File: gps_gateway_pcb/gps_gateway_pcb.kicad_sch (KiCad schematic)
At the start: 76 parts, among them J1 USB_OTG, J2 4G, J3 EG800, J4 Conn_01x03_Pin, J5 Conn_01x06_Pin, J7 SIM_Card, Q1 DTC143Z, Q2 DTC143Z, Q3 DTC143Z, Q6 2SC4617TLQ, Q7 2SC4617TLQ, SW1 RST, SW2 Boot, U1 GNSS, U2 TPS54202DDC, U3 RT9013-33GB, U4 Main, U5 ESP32-C3FH4, Y1 40MHz

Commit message: layout done go to prototype
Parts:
- removed C1, C3: 100nF, Capacitor_SMD:C_0603_1608Metric, symbol Device:C_Small
- removed C11: 10nF, Capacitor_SMD:C_0603_1608Metric, symbol Device:C
- removed C16: 10nF, Capacitor_SMD:C_0603_1608Metric, symbol Device:C_Small
- removed C17, C25: 0.1uF, Capacitor_SMD:C_0603_1608Metric, symbol Device:C_Small
- removed C23, C24: 1nF, Capacitor_SMD:C_0603_1608Metric, symbol Device:C_Small
- removed C5: 470uF, Capacitor_Tantalum_SMD:CP_EIA-7343-20_Kemet-V, symbol Device:C_Polarized_Small
- removed D4: SS34, Diode_SMD:D_SMA, symbol Diode:SS34
- removed F1: 0.35A, Fuse:Fuse_1206_3216Metric, symbol Device:Fuse_Small
- removed J4: Conn_01x03_Pin, Connector_PinHeader_1.27mm:PinHeader_1x03_P1.27mm_Vertical, symbol Connector:Conn_01x03_Pin
- removed J7: SIM_Card, UserLibrary:SIM-SMD_WL-SIM150-085, symbol UserLibrary:SIM_Card_WL-SIM150-085
- removed Q1, Q2, Q3: DTC143Z, Package_TO_SOT_SMD:SOT-416, symbol Transistor_BJT:DTC143Z
- removed Q7: 2SC4617TLQ, Package_TO_SOT_SMD:SOT-416, symbol Device:Q_NPN_BEC
- removed R1, R2: 10K, Resistor_SMD:R_0603_1608Metric, symbol Device:R
- removed R17, R20, R76: 0, Resistor_SMD:R_0603_1608Metric, symbol Device:R_Small_US
- removed R6: 100K, Resistor_SMD:R_0603_1608Metric, symbol Device:R_Small
- removed R7: 4K7, Resistor_SMD:R_0603_1608Metric, symbol Device:R
- removed R74: 10K, Resistor_SMD:R_0603_1608Metric, symbol Device:R_Small_US
- removed R8: 3K3, Resistor_SMD:R_0603_1608Metric, symbol Device:R_Small
- removed R9: 22.1K, Resistor_SMD:R_0603_1608Metric, symbol Device:R_Small
- removed SW1: RST, Button_Switch_SMD:SW_Push_SPST_NO_Alps_SKRK, symbol User Library:SW_Push
- removed SW2: Boot, Button_Switch_SMD:SW_Push_SPST_NO_Alps_SKRK, symbol User Library:SW_Push
- removed U1: GNSS, Connector_Coaxial:U.FL_Hirose_U.FL-R-SMT-1_Vertical, symbol UserLibrary:Antenna_IPEX
- removed U3: RT9013-33GB, Package_TO_SOT_SMD:TSOT-23-5, symbol UserLibrary:RT9013-33GB
- added C19: 10uF, Capacitor_SMD:C_0603_1608Metric, symbol Device:C_Small
- added D2, D3: 1N5819W, Diode_SMD:D_SOD-123, symbol Diode:SS34
- added D6: LED, LED_THT:LED_D3.0mm, symbol Device:LED
- added H1, H2: MountingHole_Pad, MountingHole:MountingHole_2.7mm_M2.5_DIN965_Pad, symbol Mechanical:MountingHole_Pad
- added J3: GNSS, Connector_Coaxial:U.FL_Hirose_U.FL-R-SMT-1_Vertical, symbol Connector:Conn_Coaxial_Small
- added J7: SIM_Card, UserLibrary:nanoSIM_ConnMold_CMNSM661004, symbol UserLibrary:SIM_Card_CD
- added JP1: SolderJumper_3_Open, Jumper:SolderJumper-3_P1.3mm_Open_Pad1.0x1.5mm, symbol Jumper:SolderJumper_3_Open
- added Q3: SS8050, Package_TO_SOT_SMD:SOT-23, symbol Device:Q_NPN_BEC
- added R1: 0R, Resistor_SMD:R_0603_1608Metric, symbol Device:R_Small_US
- added R10, R24, R25, R26, R6, R7, R8: 10K, Resistor_SMD:R_0603_1608Metric, symbol Device:R_Small_US
- added R2: 100K, Resistor_SMD:R_0603_1608Metric, symbol Device:R_Small_US
- added R3, R9: 4K7, Resistor_SMD:R_0603_1608Metric, symbol Device:R_Small_US
- added R5: 16K9, Resistor_SMD:R_0603_1608Metric, symbol Device:R_Small_US
- added TP1, TP2, TP3, TP4: TestPoint, TestPoint:TestPoint_Pad_D1.0mm, symbol Connector:TestPoint
- added U4: RT9013-33GB, Package_TO_SOT_SMD:TSOT-23-5, symbol UserLibrary:RT9013-33GB
- C1: renamed from C10; value 1uF -> 10uF
- C14: value 47uF -> 0.1uF; footprint Capacitor_SMD:C_1206_3216Metric -> Capacitor_SMD:C_0603_1608Metric; LCSC C403725 -> C1591
- C4: renamed from C2; value 0.1uF -> 10nF
- D1: value SS34 -> 1N5819W; footprint Diode_SMD:D_SMA -> Diode_SMD:D_SOD-123
- J1: renamed from J5; footprint (none) -> TerminalBlock_Phoenix:TerminalBlock_Phoenix_MPT-0,5-6-2.54_1x06_P2.54mm_Horizontal
- L2: renamed from L4; footprint Inductor_SMD:L_APV_ANR3015 -> Inductor_SMD:L_APV_ANR5040
- L3: footprint Inductor_SMD:L_0603_1608Metric -> Inductor_SMD:L_0402_1005Metric
- Q2: renamed from Q6; value 2SC4617TLQ -> SS8050; footprint Package_TO_SOT_SMD:SOT-416 -> Package_TO_SOT_SMD:SOT-23; LCSC Part #  C308648 -> (none); Mfr. Part #  2SC4617TLQ -> SS8050
- R12: renamed from R4; value 2.2K -> 4K7
- R13: renamed from R5; value 2.2K -> 4K7
- R17: renamed from R13; value 4.7K -> 4K7
- R18: renamed from R14; value 4.7K -> 4K7
- renumbered C18 to C12, C19 to C13, C22 to C15, C20 to C17, C21 to C18, C4 to C21, C7 to C23, C12 to C3, C9 to C5, C15 to C7, C13 to C9, D1 to D4, D8 to D5, D2 to D7, D3 to D8, J1 to J4, J2 to J5, J3 to J6, L2 to L1, L1 to L4, R3 to R11, R18 to R15, R19 to R16, R15 to R21, R25 to R4, U4 to U1, U5 to U3
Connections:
- net MCU_IN2 is gone; now on net Status: U3.12 (MTCK)
- net PWKEY_SIM is gone; now on net MCU_SIM_KEY: J6.7 (PWRKEY)
- net RS_TX is gone; now on net ADC_CURENT: U3.8 (GPIO3)
- net USART3_RX_SIM is gone; now on net ESP_RX_SIM: R16.1
- net USART3_TX_SIM is gone; now on net ESP_TX_SIM: Q2.2 (E)
- net ADC_CURENT: now also C14.2, R10.1, R8.2; no longer U3.6 (GPIO2)
- net BOOT: now also R7.1, TP4.1
- net ESP_RX0: now also TP1.1
- net ESP_TX0: now also TP2.1
- net GND: now also D5.1 (K), J1.4 (Pin_4), C19.1, D6.1 (K), H1.1, H2.1, J3.2 (Ext), J7.C5 (GND), J7.SH, R10.2, R5.2, U4.2 (GND); no longer J1.2 (Pin_2)
- net NET_STATUS: now also D8.1 (K)
- net RST: now also R6.1, TP3.1
- net SIM_MAIN_TX: now also Q3.2 (E)
- net SIM_STATUS: now also D7.1 (K)
- net SIM_VBAT: now also R13.2, D3.1 (K), R1.1, R2.1, U4.1 (VIN); no longer L2.2
- net Status: now also R9.1; no longer D5.1 (K), U3.4 (XTAL_32K_P)
- net USIM_CLK: now also J7.C3 (CLK)
- net USIM_DATA: now also J7.C7 (I/O)
- net USIM_DET: now also J7.CD
- net USIM_RST: now also J7.C2 (RST)
- net USIM_VDD: now also J7.C1 (VCC)
- net VCC33: now also C15.2, R12.2, R24.1, R25.1, R26.1, R3.1, R6.2, R7.2, U4.5 (VOUT)
- net at D4.2 (A): now also R3.2
- net at R4.2 (Out1): now also AE1.1 (FEED); no longer U1.1
- net at R4.3 (Out2): now also U1.1; no longer AE1.1 (FEED)
- net at D5.2 (A): now also D6.2 (A), R9.2
- net at C9.2, U2.4 (FB): now also R2.2, R5.1
- net at R18.1: now also Q3.1 (B)
- net at D1.1 (K), U2.3 (VIN): now also D2.1 (K); no longer C14.2
- net ESP_TX_SIM: now reaches U3.10 (MTDI)
- net at C23.1, L4.1: now also C19.2, J3.1 (In)
- net IO0: now reaches J1.1 (Pin_1)
- net IO0: now also U3.4 (XTAL_32K_P), R26.2
- net IO2: now reaches J1.3 (Pin_3)
- net IO2: now also U3.6 (GPIO2), R24.2
- net at J1.5 (Pin_5): now also D2.2 (A), JP1.1 (A)
- net at J1.6 (Pin_6): now also JP1.3 (B)
- removed net +3.3V_LED: R12.2, R13.2
- net RS_RX renamed ESP_RX_SIM
- net ESP_RX_SIM: now also Q3.3 (C)
- net Relay renamed IO1
- net IO1: now also J1.2 (Pin_2), R25.2
- new net: D3.2 (A), L2.2
- new net VOL_CHECK: JP1.2 (C), R1.2, R8.1
- no-connect marks 31 -> 32
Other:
- note added: "DC - DC"
- moved on the sheet: AE1, C1, C12, C13, C15, C3, C4, C5, C9, D1, D4, D5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

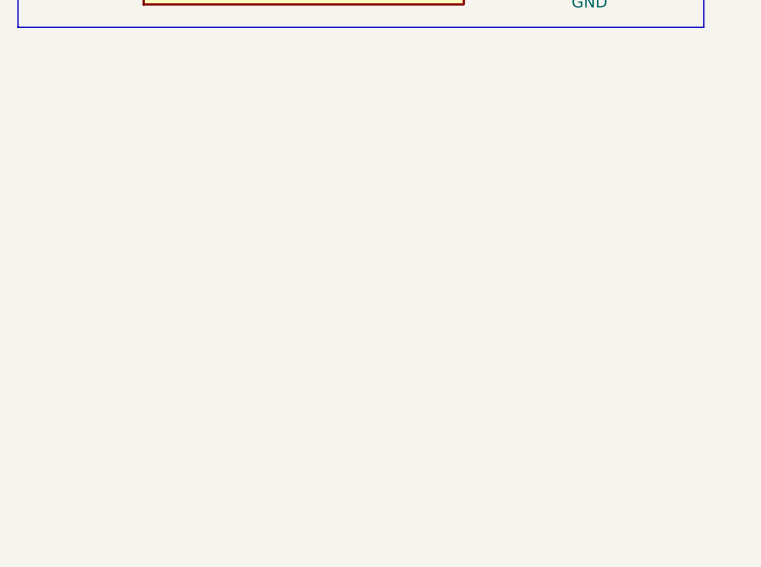
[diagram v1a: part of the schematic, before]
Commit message: add ttl2rs485 module
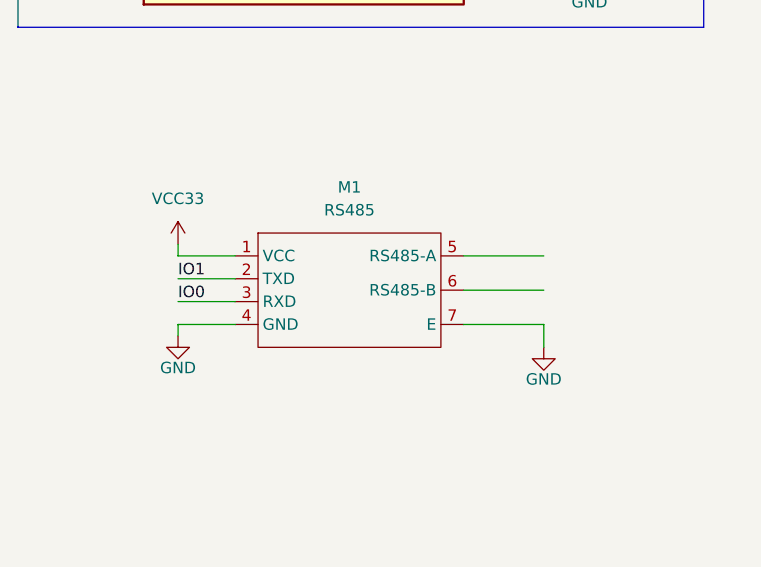
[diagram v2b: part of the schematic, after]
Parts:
- added M1: RS485, UserLibrary:Module TTL to RS485 SMD, symbol UserLibrary:TTLtoRS485
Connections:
- net GND: now also M1.4 (GND), M1.7 (E)
- net IO0: now also M1.3 (RXD)
- net IO1: now also M1.2 (TXD)
- net VCC33: now also M1.1 (VCC)

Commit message: optimize pcb
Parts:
- TP1: value TestPoint -> IO5
- TP2: value TestPoint -> IO4
- TP3: value TestPoint -> RST
- TP4: value TestPoint -> BOOT
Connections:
- net ESP_RX_SIM: now also U3.27 (U0RXD); no longer U3.9 (MTMS)
- net ESP_TX_SIM: now also U3.28 (U0TXD); no longer U3.10 (MTDI)
- net ESP_RX0 renamed IO5
- net IO5: now also U3.10 (MTDI); no longer U3.27 (U0RXD)
- net ESP_TX0 renamed IO4
- net IO4: now also U3.9 (MTMS); no longer U3.28 (U0TXD)
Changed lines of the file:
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@@
 		)
 	)
-	(label "ESP_RX0"
+	(label "IO5"
 		(at 379.73 71.12 0)
 		(effects
@@
 		)
 	)
+	(label "ESP_TX_SIM"
+		(at 280.67 69.85 0)
+		(effects
+			(font
+				(size 1.27 1.27)
+			)
+			(justify left bottom)
+		)
+	)
 	(label "SCK"
 		(at 280.67 54.61 0)
@@
 		)
 	)
-	(label "ESP_TX0"
-		(at 280.67 69.85 0)
+	(label "RST"
+		(at 354.33 54.61 180)
 		(effects
 			(font
 				(size 1.27 1.27)
 			)
-			(justify left bottom)
+			(justify right bottom)
 		)
 	)
-	(label "RST"
-		(at 354.33 54.61 180)
+	(label "ESP_RX_SIM"
+		(at 280.67 72.39 0)
 		(effects
 			(font
 				(size 1.27 1.27)
 			)
-			(justify right bottom)
+			(justify left bottom)
 		)
 	)
@@
 		)
 	)
-	(label "USIM_CLK"
-		(at 214.63 226.06 0)
+	(label "IO5"
+		(at 354.33 62.23 180)
 		(effects
 			(font
 				(size 1.27 1.27)
 			)
-			(justify left bottom)
+			(justify right bottom)
 		)
 	)
-	(label "VCC5"
-		(at 29.21 123.19 0)
+	(label "USIM_CLK"
+		(at 214.63 226.06 0)
 		(effects
 			(font
@@
 		)
 	)
-	(label "ESP_TX_SIM"
-		(at 354.33 62.23 180)
+	(label "VCC5"
+		(at 29.21 123.19 0)
 		(effects
 			(font
 				(size 1.27 1.27)
 			)
-			(justify right bottom)
+			(justify left bottom)
 		)
 	)
@@
 		)
 	)
+	(label "IO4"
+		(at 354.33 59.69 180)
+		(effects
+			(font
+				(size 1.27 1.27)
+			)
+			(justify right bottom)
+		)
+	)
 	(label "IO1"
 		(at 280.67 80.01 0)
@@
 		)
 	)
-	(label "ESP_RX_SIM"
-		(at 354.33 59.69 180)
-		(effects
-			(font
-				(size 1.27 1.27)
-			)
-			(justify right bottom)
-		)
-	)
 	(label "BOOT"
 		(at 379.73 78.74 0)
@@
 		)
 	)
-	(label "ESP_TX0"
+	(label "IO4"
 		(at 379.73 73.66 0)
 		(effects
@@
 		)
 	)
-	(label "ESP_RX0"
-		(at 280.67 72.39 0)
-		(effects
-			(font
-				(size 1.27 1.27)
-			)
-			(justify left bottom)
-		)
-	)
 	(label "USIM_RST"
 		(at 214.63 223.52 0)
@@
 			)
 		)
-		(property "Value" "TestPoint"
+		(property "Value" "BOOT"
 			(at 396.24 80.0099 90)
 			(effects
@@
 			)
 		)
-		(property "Value" "TestPoint"
+		(property "Value" "IO4"
 			(at 396.24 74.9299 90)
 			(effects
@@
 		(on_board yes)
 		(dnp no)
-		(fields_autoplaced yes)
 		(property "Reference" "TP1"
-			(at 396.24 69.8499 90)
+			(at 396.24 69.85 90)
 			(effects
 				(font
@@
 			)
 		)
-		(property "Value" "TestPoint"
+		(property "Value" "IO5"
 			(at 396.24 72.3899 90)
 			(effects
@@
 			)
 		)
-		(property "Value" "TestPoint"
+		(property "Value" "RST"
 			(at 396.24 77.4699 90)
 			(effects

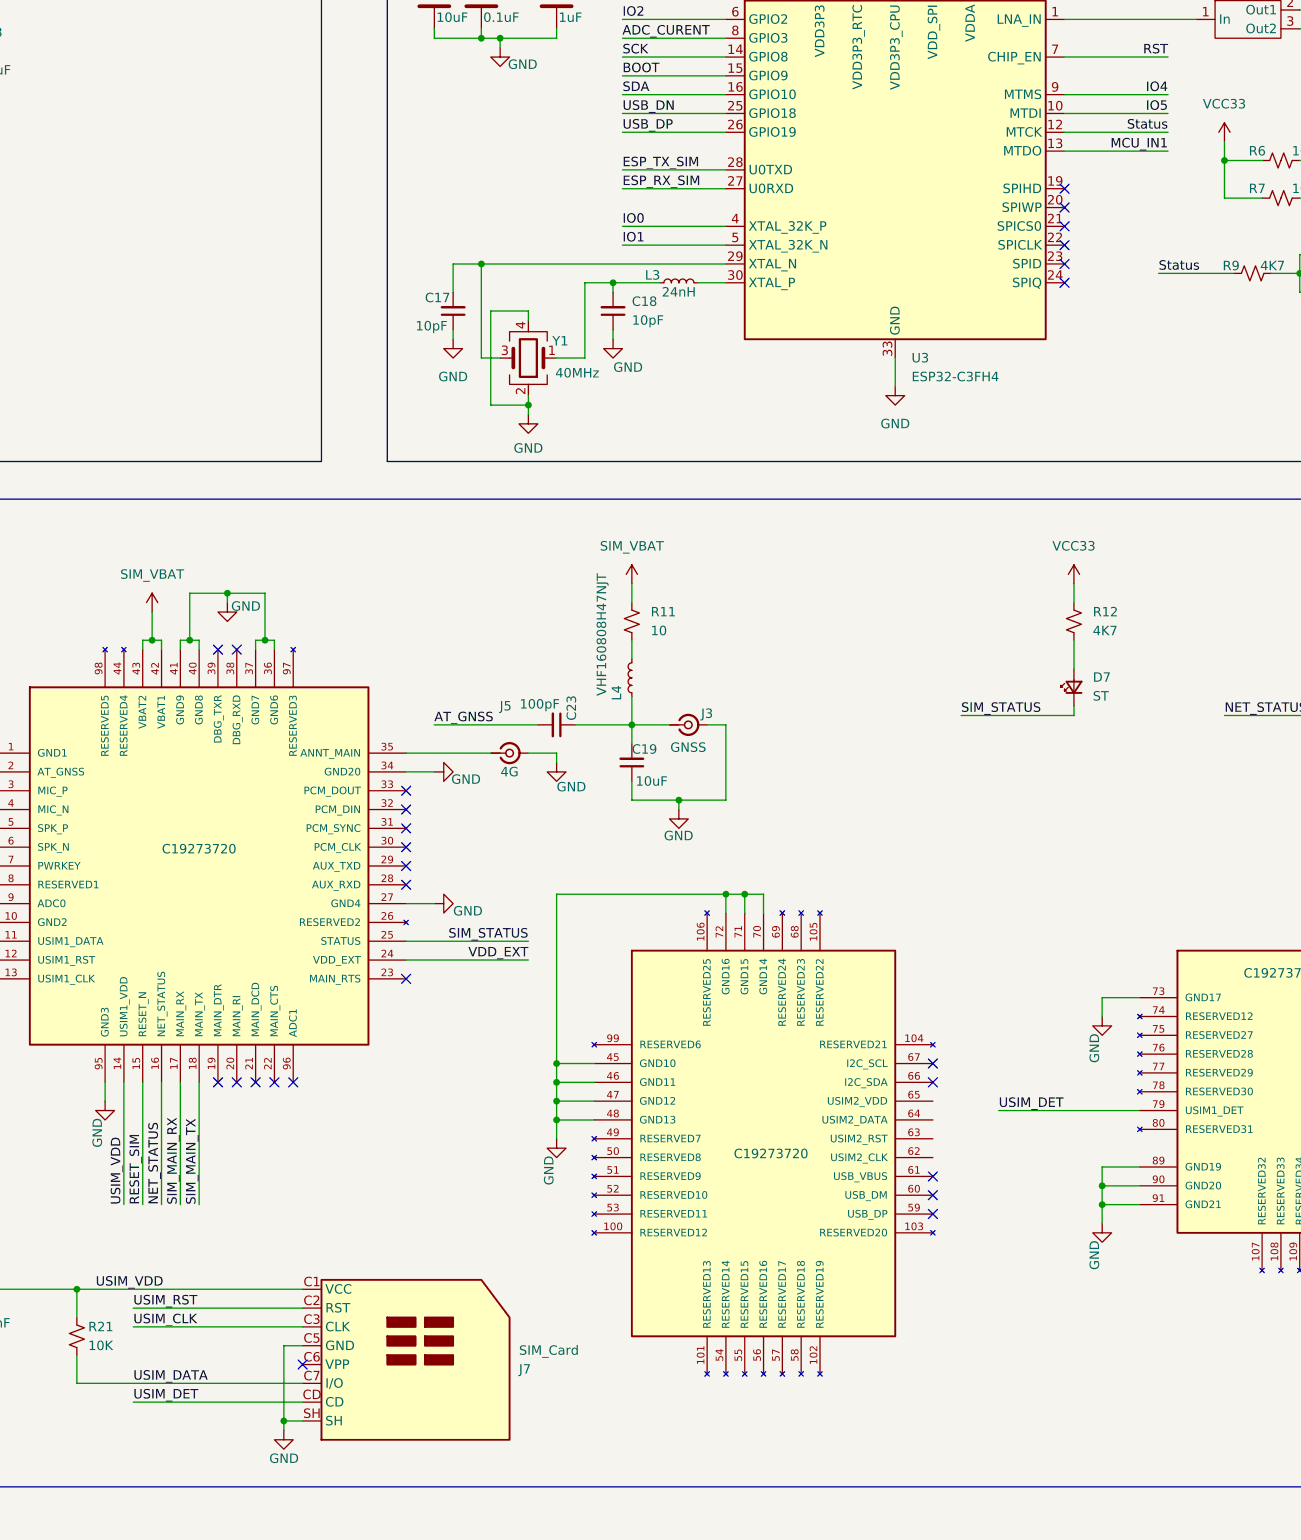
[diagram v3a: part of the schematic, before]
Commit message: change size
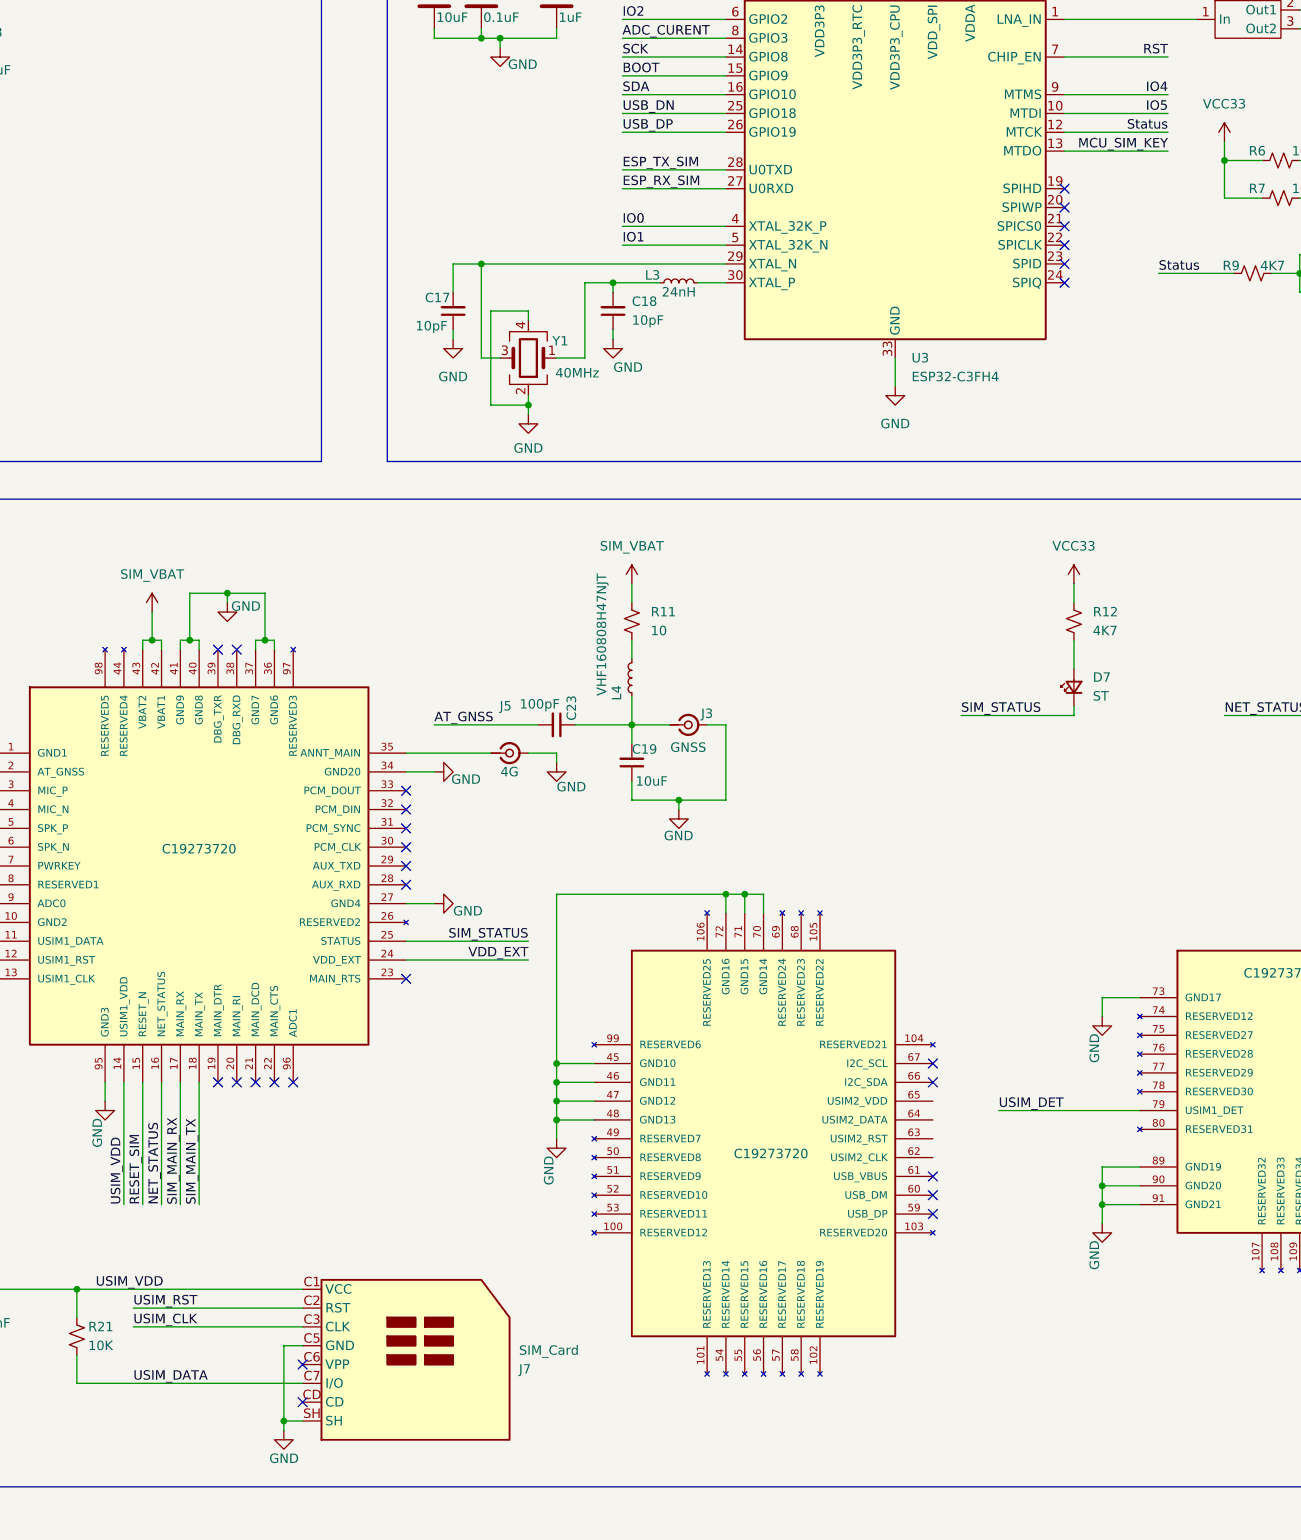
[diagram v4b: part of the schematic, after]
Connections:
- net MCU_IN1 is gone; now on net MCU_SIM_KEY: U3.13 (MTDO)
- net USIM_DET: no longer J7.CD
- no-connect marks 32 -> 33
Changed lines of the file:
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@@
 	)
 	(no_connect
+		(at 237.49 236.22)
+	)
+	(no_connect
 		(at 340.36 77.47)
 	)
@@
 	(wire
 		(pts
-			(xy 214.63 236.22) (xy 237.49 236.22)
-		)
-		(stroke
-			(width 0)
-			(type default)
-		)
-	)
-	(wire
-		(pts
 			(xy 264.16 52.07) (xy 271.78 52.07)
 		)
@@
 		)
 	)
-	(label "MCU_IN1"
-		(at 354.33 67.31 180)
+	(label "IO0"
+		(at 40.64 184.15 0)
 		(effects
 			(font
 				(size 1.27 1.27)
 			)
-			(justify right bottom)
+			(justify left bottom)
 		)
 	)
-	(label "IO0"
-		(at 40.64 184.15 0)
+	(label "MCU_SIM_KEY"
+		(at 354.33 67.31 180)
 		(effects
 			(font
 				(size 1.27 1.27)
 			)
-			(justify left bottom)
+			(justify right bottom)
 		)
 	)
@@
 		(effects
 			(font
-				(size 1.27 1.27)
-			)
-			(justify left bottom)
-		)
-	)
-	(label "USIM_DET"
-		(at 214.63 236.22 0)
-		(effects
-			(font
